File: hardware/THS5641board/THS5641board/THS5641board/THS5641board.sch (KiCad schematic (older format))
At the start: 19 parts, among them J1 Conn_01x03_Male, J2 Conn_01x03_Male, J3 Conn_02x04_Odd_Even, J4 Conn_01x20_Female, U1 AD9283

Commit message: THS5641, ADC08100, ADC08060 boards
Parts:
- removed U1: AD9283, Package_SO:SSOP-20_5.3x7.2mm_P0.65mm, symbol Analog_ADC:AD9283
- added U?: THS5641, Package_SO:TSSOP-28_4.4x9.7mm_P0.65mm, symbol kilib:THS5641
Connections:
- wire segments 111 -> 110
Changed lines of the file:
@@
 $EndDescr
-$Comp
-L Analog_ADC:AD9283 U1
-U 1 1 5DF494B5
-P 5450 2900
-F 0 "U1" H 5450 3881 50  0000 C CNN
-F 1 "AD9283" H 5450 3790 50  0000 C CNN
-F 2 "Package_SO:SSOP-20_5.3x7.2mm_P0.65mm" H 5450 2900 50  0001 C CNN
-F 3 "https://www.analog.com/media/en/technical-documentation/data-sheets/AD9283.pdf" H 5450 2900 50  0001 C CNN
-	1    5450 2900
-	1    0    0    -1
-$EndComp
 $Comp
 L Device:C C1
@@
 	5450 2000 5450 1750
 Wire Wire Line
-	5250 2100 5350 2100
-Wire Wire Line
 	5450 2100 5450 2000
-Connection ~ 5350 2100
-Wire Wire Line
-	5350 2100 5450 2100
 Connection ~ 5450 2000
 Wire Wire Line
@@
 	6800 4400 6850 4400
 NoConn ~ 7200 3900
+Wire Wire Line
+	5250 2100 5450 2100
+$Comp
+L kilib:THS5641 U?
+U 1 1 5E0E6A52
+P 5550 2500
+F 0 "U?" H 5550 1535 50  0000 C CNN
+F 1 "THS5641" H 5550 1626 50  0000 C CNN
+F 2 "Package_SO:TSSOP-28_4.4x9.7mm_P0.65mm" H 5550 2500 50  0001 C CNN
+F 3 "" H 5550 2500 50  0001 C CNN
+	1    5550 2500
+	-1   0    0    1
+$EndComp
 $EndSCHEMATC

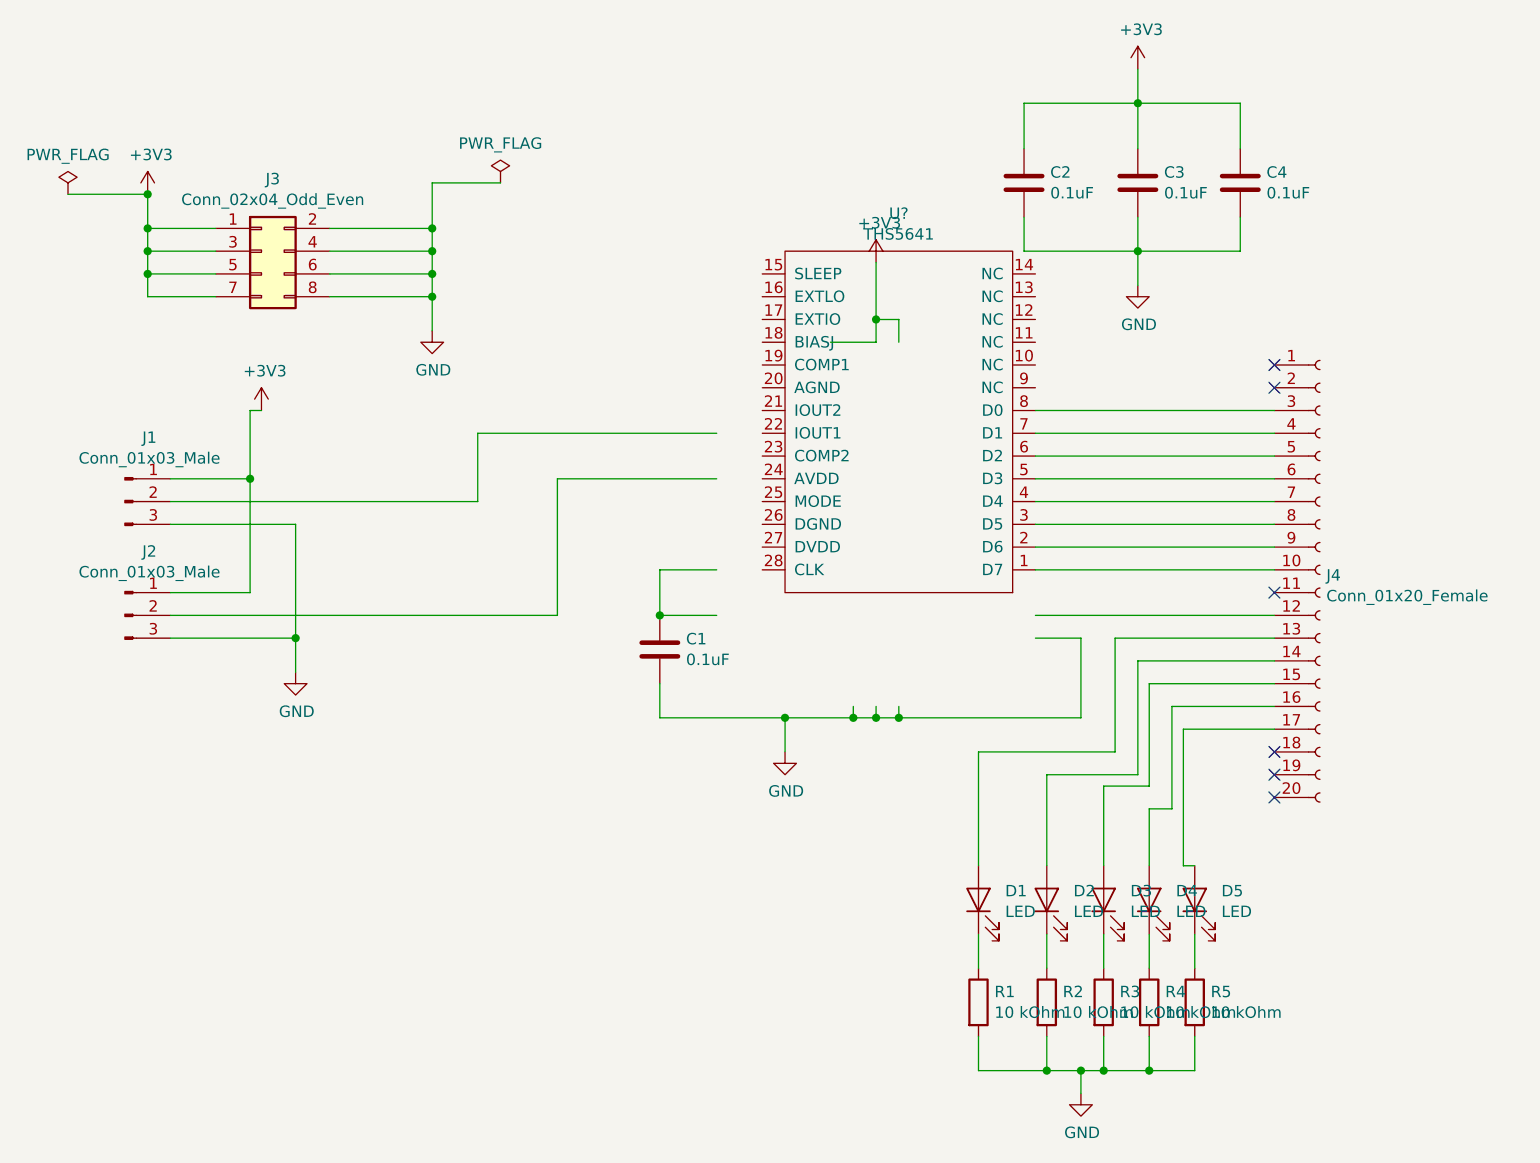
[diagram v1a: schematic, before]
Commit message: THS5641, ADC08100, ADC08060 boards
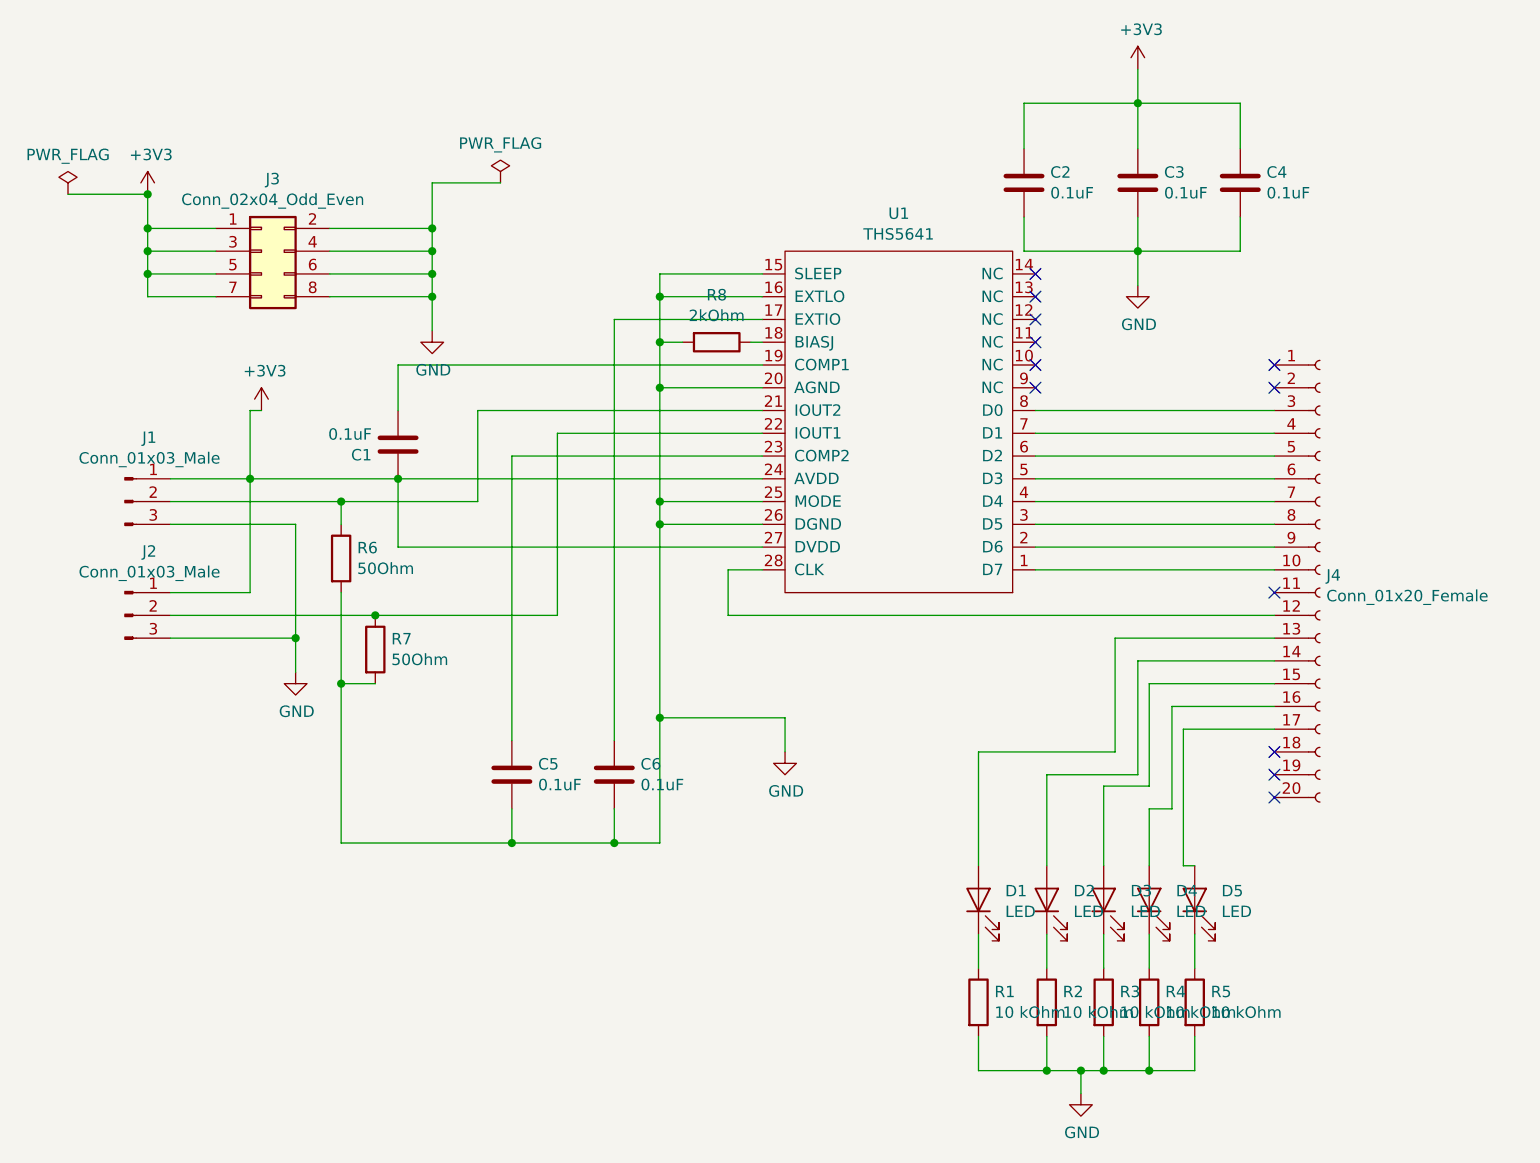
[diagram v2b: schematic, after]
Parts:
- added C5, C6: 0.1uF, Capacitor_SMD:C_0805_2012Metric, symbol Device:C
- added R6, R7: 50Ohm, Resistor_SMD:R_0805_2012Metric, symbol Device:R
- added R8: 2kOhm, Resistor_SMD:R_0805_2012Metric, symbol Device:R
- gave numbers to parts that had none: 1
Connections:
- wire segments 110 -> 129
- no-connect marks 6 -> 12
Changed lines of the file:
@@
 $EndDescr
-$Comp
-L Device:C C1
-U 1 1 5DF4A28E
-P 4500 3450
-F 0 "C1" H 4615 3496 50  0000 L CNN
-F 1 "0.1uF" H 4615 3405 50  0000 L CNN
-F 2 "Capacitor_SMD:C_0805_2012Metric" H 4538 3300 50  0001 C CNN
-F 3 "~" H 4500 3450 50  0001 C CNN
-	1    4500 3450
-	1    0    0    -1
-$EndComp
 $Comp
 L Device:C C2
@@
 Wire Wire Line
 	6600 1550 6600 1700
-Wire Wire Line
-	4500 3300 4750 3300
-Wire Wire Line
-	4750 3100 4500 3100
-Wire Wire Line
-	4500 3100 4500 3300
-Connection ~ 4500 3300
 $Comp
 L power:GND #PWR05
@@
 $EndComp
 Wire Wire Line
-	4500 3600 4500 3750
-Wire Wire Line
 	4500 3750 5050 3750
 Wire Wire Line
 	5050 3750 5050 3900
-Wire Wire Line
-	5050 3750 5350 3750
-Wire Wire Line
-	5550 3750 5550 3700
-Connection ~ 5050 3750
-Wire Wire Line
-	5450 3700 5450 3750
-Connection ~ 5450 3750
-Wire Wire Line
-	5450 3750 5550 3750
-Wire Wire Line
-	5350 3700 5350 3750
-Connection ~ 5350 3750
-Wire Wire Line
-	5350 3750 5450 3750
-$Comp
-L power:+3V3 #PWR06
-U 1 1 5DF50782
-P 5450 1750
-F 0 "#PWR06" H 5450 1600 50  0001 C CNN
-F 1 "+3V3" H 5465 1923 50  0000 C CNN
-F 2 "" H 5450 1750 50  0001 C CNN
-F 3 "" H 5450 1750 50  0001 C CNN
-	1    5450 1750
-	1    0    0    -1
-$EndComp
-Wire Wire Line
-	5550 2100 5550 2000
-Wire Wire Line
-	5550 2000 5450 2000
-Wire Wire Line
-	5450 2000 5450 1750
-Wire Wire Line
-	5450 2100 5450 2000
-Connection ~ 5450 2000
-Wire Wire Line
-	6150 3400 6350 3400
-Wire Wire Line
-	6350 3400 6350 3750
-Wire Wire Line
-	6350 3750 5550 3750
-Connection ~ 5550 3750
 $Comp
 L Connector:Conn_01x20_Female J4
@@
 Wire Wire Line
 	6150 3100 7200 3100
-Wire Wire Line
-	6150 3300 7200 3300
 $Comp
 L Connector_Generic:Conn_02x04_Odd_Even J3
@@
 	2700 2700 2700 2400
 Wire Wire Line
-	2350 2800 3700 2800
-Wire Wire Line
-	3700 2800 3700 2500
-Wire Wire Line
-	3700 2500 4750 2500
-Wire Wire Line
-	4750 2700 4050 2700
-Wire Wire Line
-	4050 2700 4050 3300
-Wire Wire Line
-	4050 3300 2350 3300
+	2350 2800 3100 2800
+Wire Wire Line
+	4050 3300 3250 3300
 NoConn ~ 7200 2200
 NoConn ~ 7200 2300
@@
 	6800 4400 6850 4400
 NoConn ~ 7200 3900
-Wire Wire Line
-	5250 2100 5450 2100
-$Comp
-L kilib:THS5641 U?
+$Comp
+L kilib:THS5641 U1
 U 1 1 5E0E6A52
 P 5550 2500
-F 0 "U?" H 5550 1535 50  0000 C CNN
+F 0 "U1" H 5550 1535 50  0000 C CNN
 F 1 "THS5641" H 5550 1626 50  0000 C CNN
 F 2 "Package_SO:TSSOP-28_4.4x9.7mm_P0.65mm" H 5550 2500 50  0001 C CNN
@@
 	-1   0    0    1
 $EndComp
+Wire Wire Line
+	4950 3100 4800 3100
+Wire Wire Line
+	4800 3100 4800 3300
+Wire Wire Line
+	4800 3300 7200 3300
+Wire Wire Line
+	3700 2400 4950 2400
+Wire Wire Line
+	3700 2400 3700 2800
+Wire Wire Line
+	4050 2500 4950 2500
+Wire Wire Line
+	4050 2500 4050 3300
+Wire Wire Line
+	4950 1800 4500 1800
+Wire Wire Line
+	4500 1800 4500 1900
+Wire Wire Line
+	4500 1900 4950 1900
+Connection ~ 4500 1900
+Wire Wire Line
+	4500 1900 4500 2100
+$Comp
+L Device:C C1
+U 1 1 5E108A69
+P 3350 2550
+F 0 "C1" H 3465 2596 50  0000 L CNN
+F 1 "0.1uF" H 3465 2505 50  0000 L CNN
+F 2 "Capacitor_SMD:C_0805_2012Metric" H 3388 2400 50  0001 C CNN
+F 3 "~" H 3350 2550 50  0001 C CNN
+	1    3350 2550
+	-1   0    0    1
+$EndComp
+$Comp
+L Device:C C5
+U 1 1 5E108A6F
+P 3850 4000
+F 0 "C5" H 3965 4046 50  0000 L CNN
+F 1 "0.1uF" H 3965 3955 50  0000 L CNN
+F 2 "Capacitor_SMD:C_0805_2012Metric" H 3888 3850 50  0001 C CNN
+F 3 "~" H 3850 4000 50  0001 C CNN
+	1    3850 4000
+	1    0    0    -1
+$EndComp
+$Comp
+L Device:C C6
+U 1 1 5E108A75
+P 4300 4000
+F 0 "C6" H 4415 4046 50  0000 L CNN
+F 1 "0.1uF" H 4415 3955 50  0000 L CNN
+F 2 "Capacitor_SMD:C_0805_2012Metric" H 4338 3850 50  0001 C CNN
+F 3 "~" H 4300 4000 50  0001 C CNN
+	1    4300 4000
+	1    0    0    -1
+$EndComp
+Wire Wire Line
+	4300 4300 4300 4150
+Wire Wire Line
+	3850 4150 3850 4300
+Wire Wire Line
+	3850 4300 4300 4300
+Wire Wire Line
+	4500 3750 4500 4300
+Wire Wire Line
+	4500 4300 4300 4300
+Connection ~ 4500 3750
+Connection ~ 4300 4300
+Wire Wire Line
+	4950 2000 4300 2000
+Wire Wire Line
+	4300 2000 4300 3850
+Wire Wire Line
+	4950 2600 3850 2600
+Wire Wire Line
+	2700 2700 3350 2700
+Wire Wire Line
+	3350 2200 3350 2400
+Wire Wire Line
+	3350 2200 4950 2200
+Wire Wire Line
+	3850 2600 3850 3850
+Wire Wire Line
+	4950 2300 4500 2300
+Connection ~ 4500 2300
+Wire Wire Line
+	4500 2300 4500 2800
+Wire Wire Line
+	4950 2800 4500 2800
+Connection ~ 4500 2800
+Wire Wire Line
+	4500 2800 4500 2900
+Wire Wire Line
+	4950 2900 4500 2900
+Connection ~ 4500 2900
+Wire Wire Line
+	4500 2900 4500 3750
+$Comp
+L Device:R R8
+U 1 1 5E14B7D4
+P 4750 2100
+F 0 "R8" V 4543 2100 50  0000 C CNN
+F 1 "2kOhm" V 4634 2100 50  0000 C CNN
+F 2 "Resistor_SMD:R_0805_2012Metric" V 4680 2100 50  0001 C CNN
+F 3 "~" H 4750 2100 50  0001 C CNN
+	1    4750 2100
+	0    1    1    0
+$EndComp
+Wire Wire Line
+	4900 2100 4950 2100
+Wire Wire Line
+	4600 2100 4500 2100
+Connection ~ 4500 2100
+Wire Wire Line
+	4500 2100 4500 2300
+Wire Wire Line
+	4950 2700 3350 2700
+Connection ~ 3350 2700
+Wire Wire Line
+	4950 3000 3350 3000
+Wire Wire Line
+	3350 3000 3350 2700
+$Comp
+L Device:R R7
+U 1 1 5E15FFAB
+P 3250 3450
+F 0 "R7" H 3320 3496 50  0000 L CNN
+F 1 "50Ohm" H 3320 3405 50  0000 L CNN
+F 2 "Resistor_SMD:R_0805_2012Metric" V 3180 3450 50  0001 C CNN
+F 3 "~" H 3250 3450 50  0001 C CNN
+	1    3250 3450
+	1    0    0    -1
+$EndComp
+Connection ~ 3250 3300
+Wire Wire Line
+	3250 3300 2350 3300
+$Comp
+L Device:R R6
+U 1 1 5E160852
+P 3100 3050
+F 0 "R6" H 3170 3096 50  0000 L CNN
+F 1 "50Ohm" H 3170 3005 50  0000 L CNN
+F 2 "Resistor_SMD:R_0805_2012Metric" V 3030 3050 50  0001 C CNN
+F 3 "~" H 3100 3050 50  0001 C CNN
+	1    3100 3050
+	1    0    0    -1
+$EndComp
+Wire Wire Line
+	3100 2800 3100 2900
+Connection ~ 3100 2800
+Wire Wire Line
+	3100 2800 3700 2800
+Wire Wire Line
+	3100 4300 3850 4300
+Connection ~ 3850 4300
+Wire Wire Line
+	3100 3200 3100 3600
+Wire Wire Line
+	3250 3600 3100 3600
+Connection ~ 3100 3600
+Wire Wire Line
+	3100 3600 3100 4300
+NoConn ~ 6150 1800
+NoConn ~ 6150 1900
+NoConn ~ 6150 2000
+NoConn ~ 6150 2100
+NoConn ~ 6150 2200
+NoConn ~ 6150 2300
 $EndSCHEMATC
